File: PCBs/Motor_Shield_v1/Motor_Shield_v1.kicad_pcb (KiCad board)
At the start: 4 copper layers, 68.6 x 53.3 mm, 30 parts, among them J1 Power, J2 Digital/PWM, J3 Analog, J4 Digital/PWM

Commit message: Update PCB
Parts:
- R1: value 2,7kΩ -> 1.8
- R4: value 2,7kΩ -> 1.8kΩ
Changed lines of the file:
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@@
 		(tags "Resistor Axial_DIN0207 series Axial Horizontal pin pitch 7.62mm 0.25W = 1/4W length 6.3mm diameter 2.5mm")
 		(property "Reference" "R6"
-			(at 3.81 -2.37 90)
+			(at 3.81 2.5 90)
 			(layer "F.SilkS")
 			(effects
@@
 		)
 		(property "Value" "220Ω"
-			(at 3.81 2.37 90)
+			(at 4 -2.5 90)
 			(layer "F.Fab")
 			(effects
@@
 			)
 		)
-		(property "Value" "2,7kΩ"
+		(property "Value" "1.8"
 			(at 3.81 2.37 0)
 			(layer "F.Fab")
@@
 			)
 		)
-		(property "Value" "2,7kΩ"
+		(property "Value" "1.8kΩ"
 			(at 3.81 -2 0)
 			(layer "F.Fab")

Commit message: update PCB
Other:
- board text added: "MotorShield v1"
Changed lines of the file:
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@@
 		(layer "Edge.Cuts")
+	)
+	(gr_text "MotorShield v1"
+		(at 101 49.5 0)
+		(layer "F.SilkS")
+		(effects
+			(font
+				(size 1 1)
+				(thickness 0.15)
+			)
+			(justify left bottom)
+		)
 	)
 	(gr_text "ICSP"

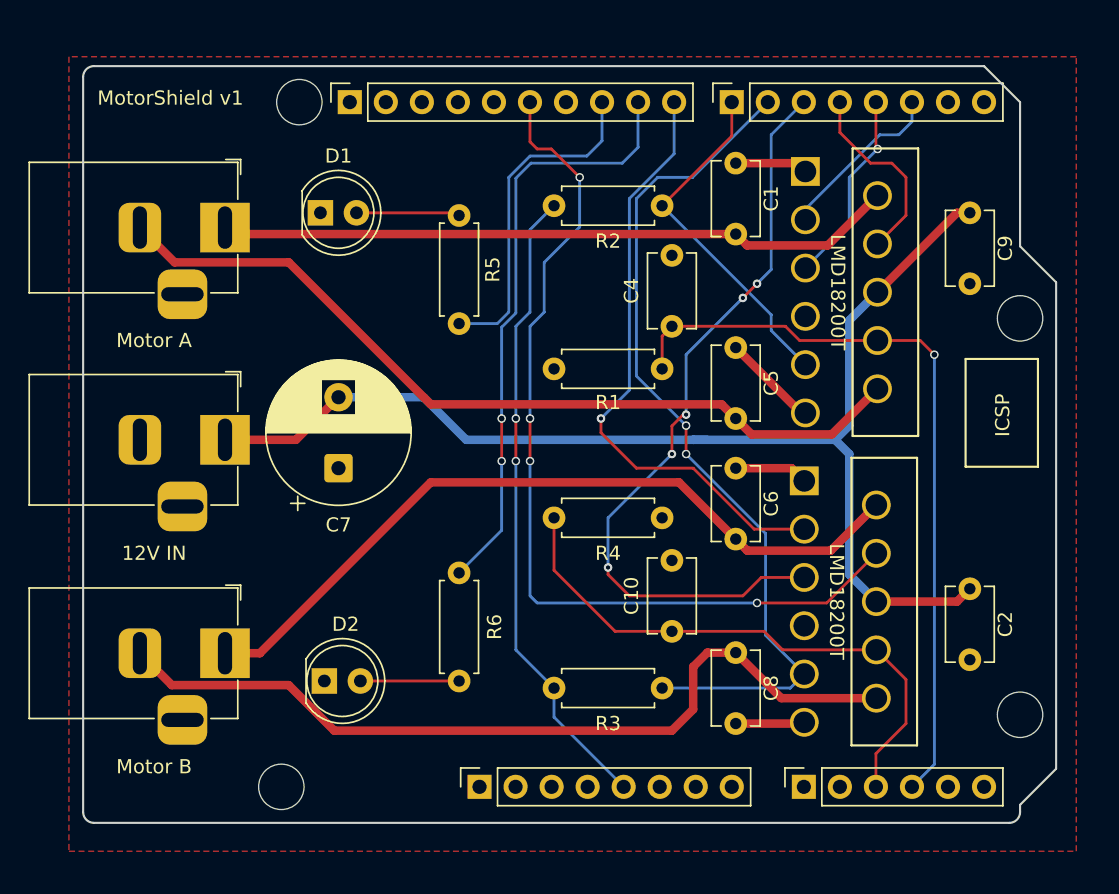
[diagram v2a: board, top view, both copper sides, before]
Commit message: Redesign MotorShield
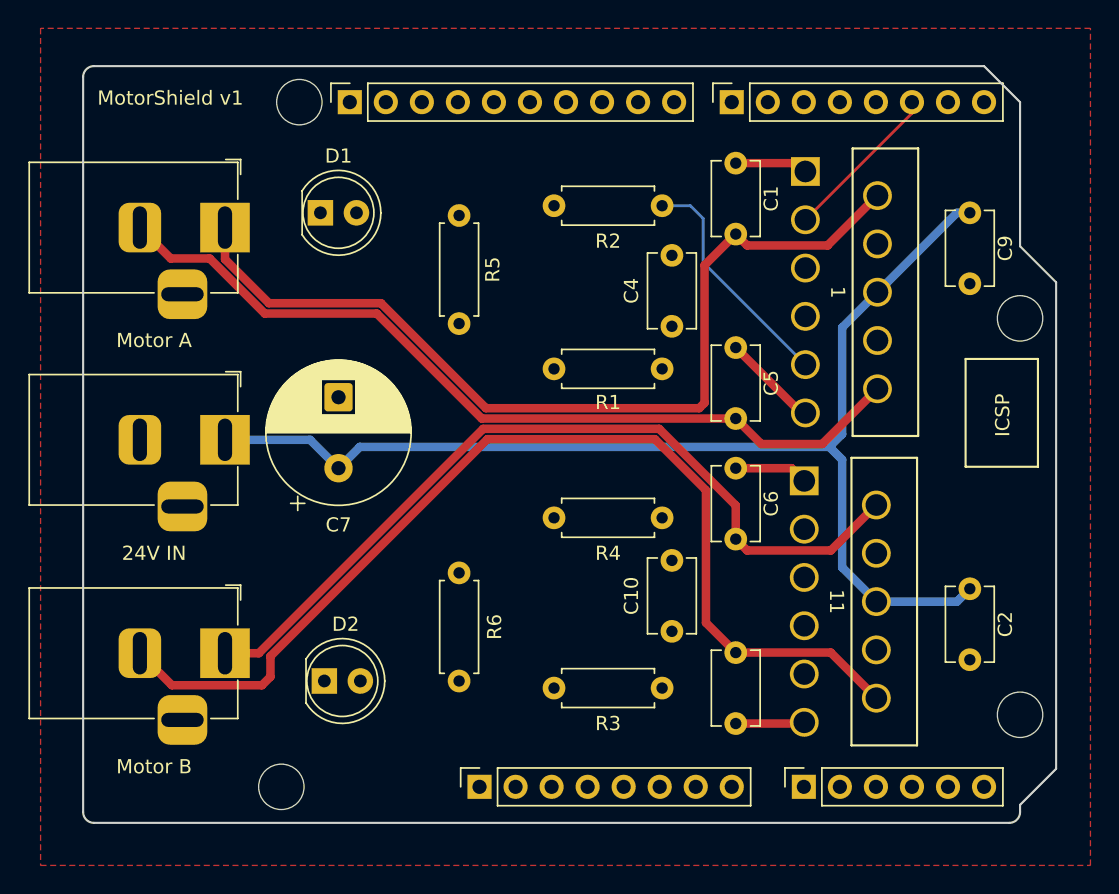
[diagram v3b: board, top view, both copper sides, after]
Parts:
- added G***: LOGO, LOGO, B.Cu at (105.8, 50.9)
- 24V IN: renamed from 12V IN
- D1: value Motor A -> TEMP_WARN
- D2: value Motor B -> TEMP_WARN
- R1: value 1.8 -> 1.8kΩ
- renumbered LMD18200T to 1, LMD18200T to 11
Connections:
- 1 pad 6: +12V -> +24V
- 11 pad 6: +12V -> +24V
- 24V IN pad 1: +12V -> +24V
- C2 pad 1: +12V -> +24V
- C7 pad 1: GND -> +24V
- C7 pad 2: +12V -> GND
- C9 pad 1: +12V -> +24V
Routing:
- net +12V: track 86.5 -> 0.00 mm
- net +24V: track 0.00 -> 84.4 mm
- net /12: track 64.4 -> 45.3 mm, vias 4 -> 0
- net /*5: track 54.1 -> 36.3 mm, vias 5 -> 0
- net Net-(1-OUT_1): track 48.0 -> 65.1 mm
- net Net-(11-OUT_2): track 59.5 -> 73.9 mm
- net /*6: track 60.9 -> 51.8 mm, vias 2 -> 0
- net Net-(11-OUT_1): track 54.2 -> 60.0 mm
- net /8: track 42.6 -> 37.2 mm, vias 1 -> 0
- net +5V: track 45.2 -> 49.1 mm, vias 2 -> 0
- net /A3: track 53.7 -> 50.7 mm, vias 1 -> 0
- net /4: track 13.6 -> 11.1 mm
- net /A2: track 40.4 -> 38.0 mm
- net /7: track 24.7 -> 25.9 mm
- net /*10: track 23.7 -> 22.9 mm
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
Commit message: Set JLC Label Position
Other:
- board text added: "JLCJLCJLCJLC"
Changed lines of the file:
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@@
+		)
+	)
+	(gr_text "JLCJLCJLCJLC"
+		(at 111.9 99 0)
+		(layer "B.SilkS")
+		(effects
+			(font
+				(size 1 1)
+				(thickness 0.15)
+			)
+			(justify left bottom mirror)
 		)
 	)

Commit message: Final Touches
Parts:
- added G***: LOGO, LOGO, B.Cu at (161.3, 73.5)
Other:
- board text added: "Designed in Switzerland"
